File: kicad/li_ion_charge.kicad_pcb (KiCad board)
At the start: 2 copper layers, 17 parts, among them P101 USB_B, P102 CONN_01X02, P103 CONN_01X02, U101 MCP73834-FCI/UN

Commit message: Final USB footprint and added a label to schematic
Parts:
- P101: footprint li_ion_charge_library:USB_Micro-B -> li_ion_charge_library:USB_Micro-B_10118193-0001LF
- moved P101 1.35 mm to (158.2, 87.9)
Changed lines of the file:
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@@
 (kicad_pcb (version 4) (host pcbnew 4.0.6-e0-6349~53~ubuntu14.04.1)
   (general
-    (links 35)
-    (no_connects 35)
+    (links 37)
+    (no_connects 37)
     (area 0 0 0 0)
     (thickness 1.6)
@@
     )
   )
-  (module li_ion_charge_library:USB_Micro-B (layer F.Cu)
-    (at 158.2 89.275 180)
+  (module li_ion_charge_library:USB_Micro-B_10118193-0001LF (layer F.Cu)
+    (at 158.225 87.925 180)
     (descr "Micro USB Type B Receptacle")
     (tags "USB USB_B USB_micro USB_OTG")
     (attr smd)
-    (fp_text reference P101 (at 0.0254 -4.6116 180) (layer F.SilkS)
-      (effects (font (size 1 1) (thickness 0.15)))
-    )
-    (fp_text value USB_B (at 0.0254 3.6384 180) (layer F.Fab)
-      (effects (font (size 1 1) (thickness 0.15)))
-    )
-    (fp_line (start -4.5746 -3.9616) (end 4.6254 -3.9616) (layer F.CrtYd) (width 0.05))
-    (fp_line (start 4.6254 -3.9616) (end 4.6254 2.8884) (layer F.CrtYd) (width 0.05))
-    (fp_line (start 4.6254 2.8884) (end -4.5746 2.8884) (layer F.CrtYd) (width 0.05))
-    (fp_line (start -4.5746 2.8884) (end -4.5746 -3.9616) (layer F.CrtYd) (width 0.05))
-    (fp_line (start -4.3246 2.6584) (end 4.3754 2.6584) (layer F.SilkS) (width 0.12))
-    (fp_line (start -4.3246 -3.7516) (end 4.3754 -3.7516) (layer F.SilkS) (width 0.12))
-    (fp_line (start 4.3754 -3.7516) (end 4.3754 2.6584) (layer F.SilkS) (width 0.12))
-    (fp_line (start 4.3754 1.4284) (end -4.3246 1.4284) (layer F.SilkS) (width 0.12))
-    (fp_line (start -4.3246 2.6584) (end -4.3246 -3.7516) (layer F.SilkS) (width 0.12))
-    (pad 6 smd rect (at 1.2 0 270) (size 1.8 1.9) (layers F.Cu F.Paste F.Mask)
-      (net 1 GND))
-    (pad 6 smd rect (at -1.2 0 270) (size 1.8 1.9) (layers F.Cu F.Paste F.Mask)
+    (fp_text reference P101 (at -5.7785 -2.3876 450) (layer F.SilkS)
+      (effects (font (size 1 1) (thickness 0.15)))
+    )
+    (fp_text value USB_B (at 5.775 -1.6 270) (layer F.Fab)
+      (effects (font (size 1 1) (thickness 0.15)))
+    )
+    (fp_line (start -5 -5) (end 5 -5) (layer Eco1.User) (width 0.12))
+    (fp_line (start 5 -5) (end 5 1.45) (layer Eco1.User) (width 0.12))
+    (fp_line (start 5 1.45) (end -5 1.45) (layer Eco1.User) (width 0.12))
+    (fp_line (start -5 1.45) (end -5 -5) (layer Eco1.User) (width 0.12))
+    (pad 6 smd rect (at 1.2 0 270) (size 1.89 1.9) (layers F.Cu F.Paste F.Mask)
+      (net 1 GND))
+    (pad 6 smd rect (at -1.2 0 270) (size 1.89 1.9) (layers F.Cu F.Paste F.Mask)
       (net 1 GND))
     (pad 1 smd rect (at -1.3 -2.675 270) (size 1.35 0.4) (layers F.Cu F.Paste F.Mask)
@@
     (pad 6 smd rect (at 3.2 -2.45 270) (size 1.4 1.6) (layers F.Cu F.Paste F.Mask)
       (net 1 GND))
-    (pad 6 thru_hole oval (at -3.3 0 270) (size 1.6 0.9) (drill oval 1.2 0.5) (layers *.Cu *.Mask)
-      (net 1 GND))
-    (pad 6 thru_hole oval (at 3.3 0 270) (size 1.6 0.9) (drill oval 1.2 0.5) (layers *.Cu *.Mask)
-      (net 1 GND))
-  )
+    (pad 6 thru_hole circle (at -3.3 0 270) (size 1.6 1.6) (drill 1.2) (layers *.Cu *.Mask)
+      (net 1 GND))
+    (pad 6 thru_hole circle (at 3.3 0 270) (size 1.6 1.6) (drill 1.2) (layers *.Cu *.Mask)
+      (net 1 GND))
+  )

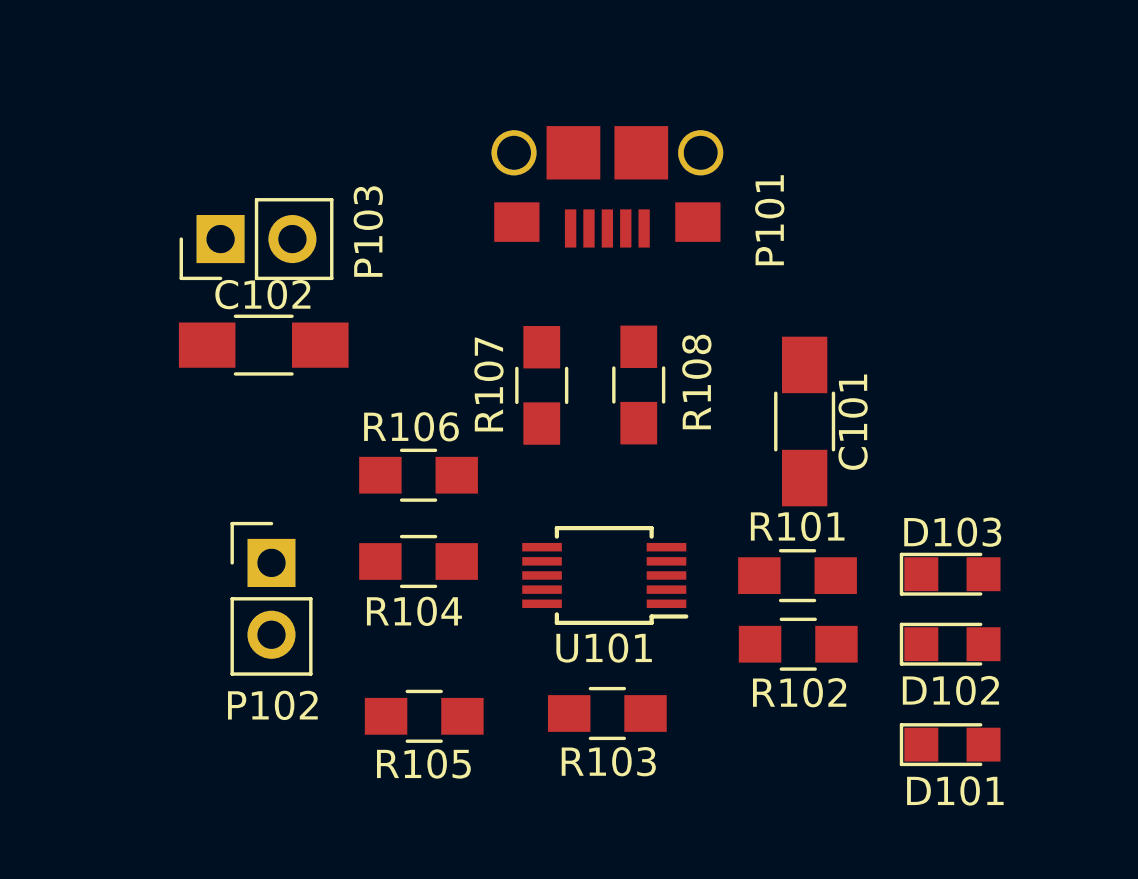
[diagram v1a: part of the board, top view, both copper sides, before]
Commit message: Update schematic and netlist to include a new nopop resistor, and this should be close to what the final part placement on the layout should look like
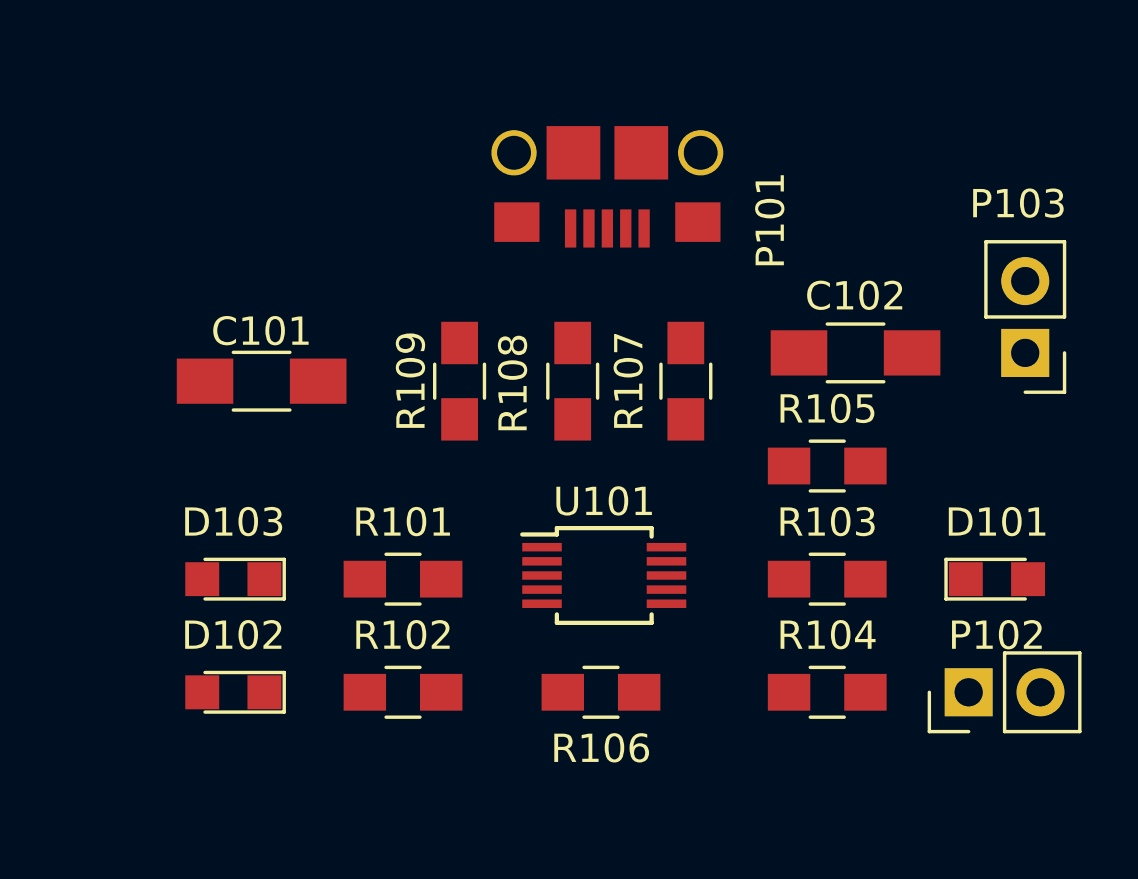
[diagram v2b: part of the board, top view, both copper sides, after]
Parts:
- added R109: NOPOP, Resistors_SMD:R_0805_HandSoldering, F.Cu at (153.0, 96.0)
- moved P103 28.7 mm to (173.0, 95.0), turned to 180 degrees
- moved D102 25.5 mm to (145.0, 107.0), turned to 180 degrees
- moved D103 25.4 mm to (145.0, 103.0), turned to 180 degrees
- moved P102 25.1 mm to (171.0, 107.0), turned to 90 degrees
- moved C102 20.9 mm to (167.0, 95.0), turned to 180 degrees
- moved C101 19.3 mm to (146.0, 96.0), turned to 0 degrees
- moved R105 16.8 mm to (166.0, 99.0), turned to 180 degrees
- moved R104 15.2 mm to (166.0, 107.0), turned to 0 degrees
- moved R102 14.1 mm to (151.0, 107.0), turned to 180 degrees
- moved R101 14.0 mm to (151.0, 103.0), turned to 180 degrees
- moved R106 10.0 mm to (158.0, 107.0)
- moved R103 9.11 mm to (166.0, 103.0)
- moved D101 6.06 mm to (172.0, 103.0)
- moved R107 5.10 mm to (161.0, 96.0), turned to 90 degrees
- moved R108 2.34 mm to (157.0, 96.0), turned to 90 degrees
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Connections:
- P101 pad 4: GND -> Net-(P101-Pad4)
